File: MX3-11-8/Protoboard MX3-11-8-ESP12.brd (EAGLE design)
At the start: 74 x 99.4 mm, 638 parts, among them J1 DCJ0202, X3 RJ45

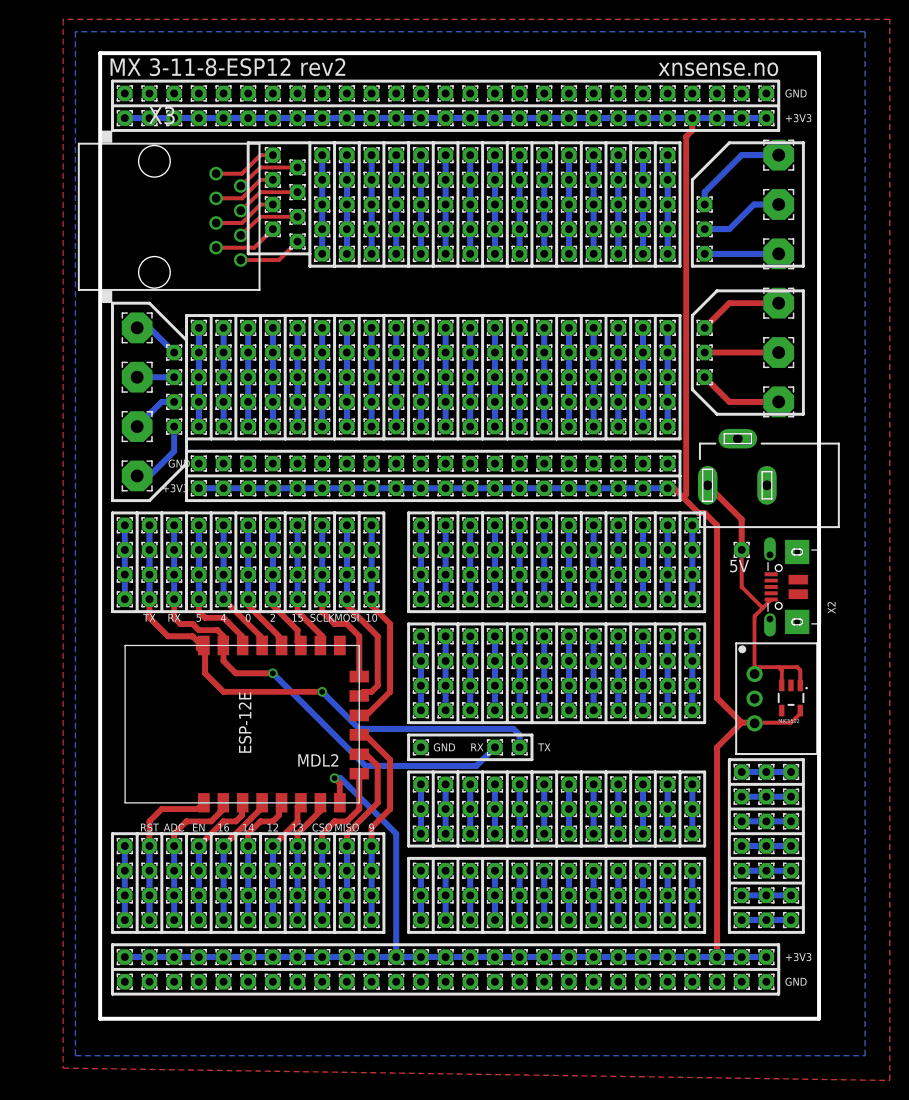
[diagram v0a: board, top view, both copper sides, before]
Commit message: Adjusted Polygon
Adjusted Polygon on all boxes. Changed length on MX-4-7-6 to fit the
box, it was 2mm to long.
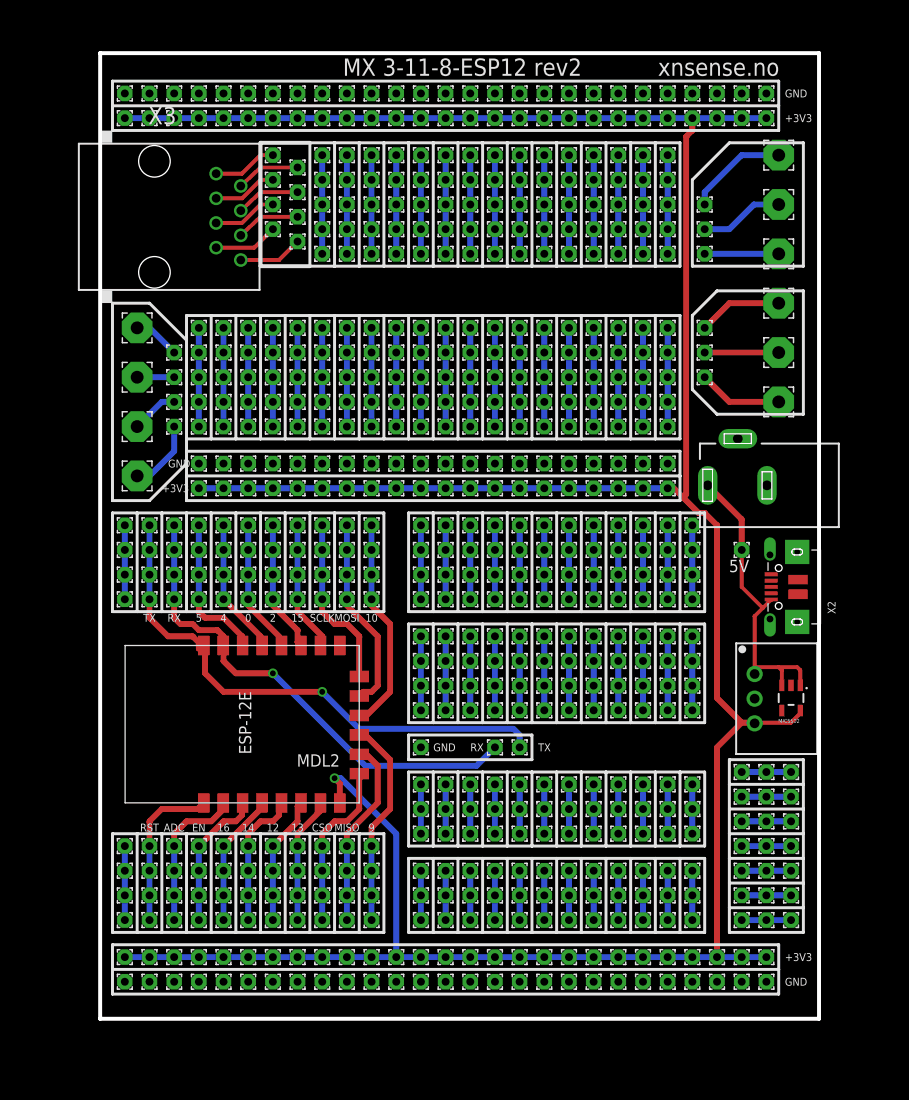
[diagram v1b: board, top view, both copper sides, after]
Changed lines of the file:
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@@
 <setting verticaltext="up"/>
 </settings>
-<grid distance="50" unitdist="mil" unit="mil" style="dots" multiple="1" display="yes" altdistance="5" altunitdist="mil" altunit="mil"/>
+<grid distance="50" unitdist="mil" unit="mil" style="dots" multiple="1" display="yes" altdistance="25" altunitdist="mil" altunit="mil"/>
 <layers>
 <layer number="1" name="Top" color="4" fill="1" visible="yes" active="yes"/>
@@
 <wire x1="74" y1="99.4" x2="74" y2="0" width="0.4064" layer="20"/>
 <text x="69.915" y="98.845" size="1.778" layer="25" rot="R180">xnsense.no</text>
-<text x="25.455" y="98.845" size="1.778" layer="25" rot="R180">MX 3-11-8-ESP12 rev2</text>
+<text x="49.585" y="98.845" size="1.778" layer="25" rot="R180">MX 3-11-8-ESP12 rev2</text>
 <wire x1="1.27" y1="96.52" x2="1.27" y2="93.98" width="0.3048" layer="25"/>
 <wire x1="1.27" y1="93.98" x2="69.85" y2="93.98" width="0.3048" layer="25"/>
@@
 <wire x1="1.27" y1="91.44" x2="69.85" y2="91.44" width="0.3048" layer="25"/>
 <wire x1="69.85" y1="91.44" x2="69.85" y2="93.98" width="0.3048" layer="25"/>
-<wire x1="15.24" y1="90.17" x2="21.59" y2="90.17" width="0.3048" layer="25"/>
-<wire x1="21.59" y1="90.17" x2="21.59" y2="78.74" width="0.3048" layer="25"/>
-<wire x1="21.59" y1="78.74" x2="15.24" y2="78.74" width="0.3048" layer="25"/>
-<wire x1="15.24" y1="78.74" x2="15.24" y2="90.17" width="0.3048" layer="25"/>
+<wire x1="21.59" y1="90.17" x2="21.59" y2="77.47" width="0.3048" layer="25"/>
 <wire x1="21.59" y1="90.17" x2="24.13" y2="90.17" width="0.3048" layer="25"/>
 <wire x1="24.13" y1="90.17" x2="24.13" y2="77.47" width="0.3048" layer="25"/>
 <wire x1="24.13" y1="77.47" x2="21.59" y2="77.47" width="0.3048" layer="25"/>
-<wire x1="21.59" y1="77.47" x2="21.59" y2="78.74" width="0.3048" layer="25"/>
 <wire x1="24.13" y1="77.47" x2="26.67" y2="77.47" width="0.3048" layer="25"/>
 <wire x1="26.67" y1="77.47" x2="29.21" y2="77.47" width="0.3048" layer="25"/>
@@
 <text x="6.35" y="54.61" size="0.8128" layer="25" align="center-left">+3V3</text>
 <text x="6.985" y="57.15" size="0.8128" layer="25" align="center-left">GND</text>
+<wire x1="21.59" y1="90.17" x2="16.51" y2="90.17" width="0.4064" layer="25"/>
+<wire x1="21.59" y1="77.47" x2="16.51" y2="77.47" width="0.4064" layer="25"/>
+<wire x1="16.51" y1="90.17" x2="16.51" y2="77.47" width="0.4064" layer="25"/>
+<dimension x1="0" y1="0" x2="0" y2="99.4" x3="-5.08" y3="49.7" textsize="1.778" layer="47"/>
+<dimension x1="0" y1="99.4" x2="74" y2="99.4" x3="37" y3="102.87" textsize="1.778" layer="47"/>
+<dimension x1="69.85" y1="96.52" x2="69.85" y2="99.4" x3="76.2" y3="97.96" textsize="1.778" layer="47"/>
+<dimension x1="69.85" y1="2.54" x2="69.85" y2="0" x3="77.47" y3="1.27" textsize="1.778" layer="47"/>
 </plain>
 <attributes>
@@
 <contactref element="DC" pad="2"/>
 <polygon width="0.4064" layer="1">
-<vertex x="-3.81" y="102.87"/>
-<vertex x="-3.81" y="-5.08"/>
-<vertex x="81.28" y="-6.35"/>
-<vertex x="81.28" y="102.87"/>
+<vertex x="0" y="99.4"/>
+<vertex x="0" y="0"/>
+<vertex x="74" y="0"/>
+<vertex x="74" y="99.4"/>
 </polygon>
 <contactref element="PAD27" pad="1"/>
@@
 <signal name="N$1">
 <polygon width="0.6096" layer="16">
-<vertex x="-2.54" y="101.6"/>
-<vertex x="-2.54" y="-3.81"/>
-<vertex x="78.74" y="-3.81"/>
-<vertex x="78.74" y="101.6"/>
+<vertex x="0" y="99.4"/>
+<vertex x="0" y="0"/>
+<vertex x="74" y="0"/>
+<vertex x="74" y="99.4"/>
 </polygon>
 </signal>

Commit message: Update to rev2
Updated to Pin headers instead of single wire pads
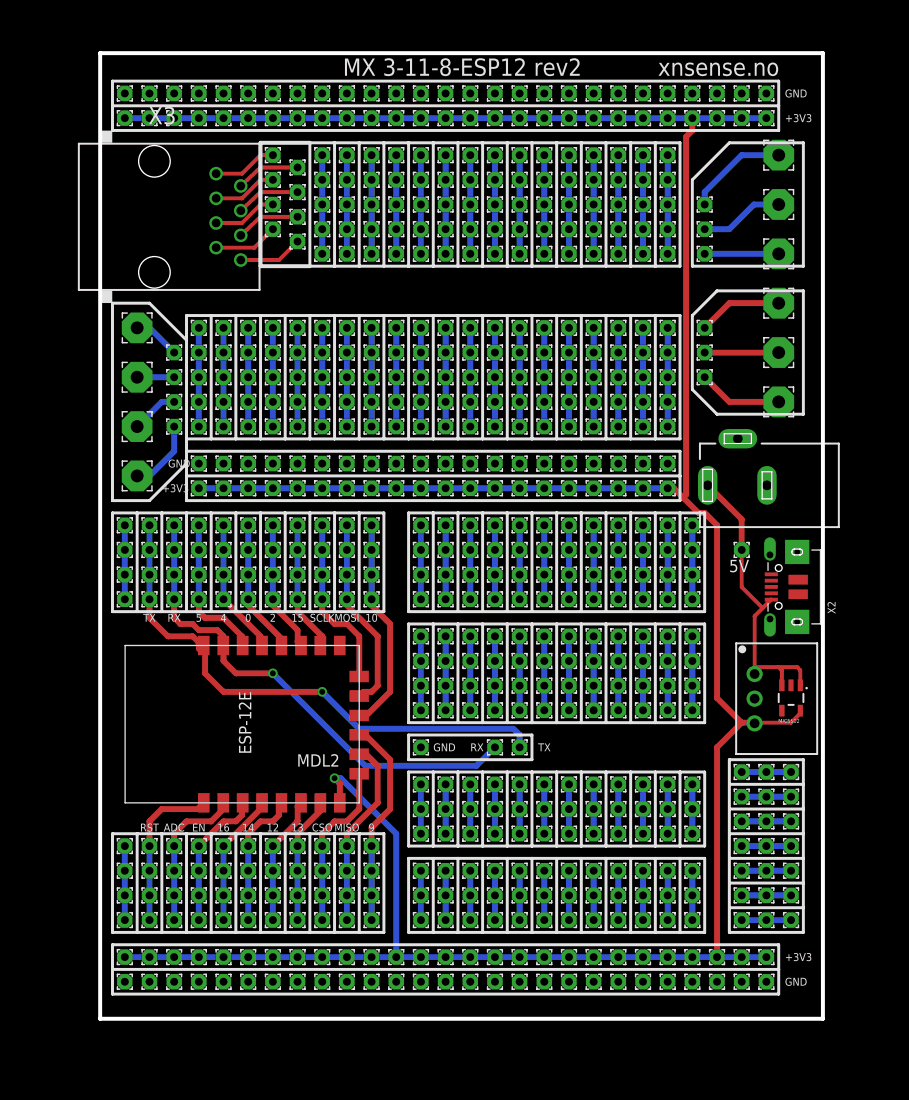
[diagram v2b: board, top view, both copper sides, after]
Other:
- board size 74 x 99.4 mm -> 74.4 x 99.4 mm
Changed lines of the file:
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@@
 <setting verticaltext="up"/>
 </settings>
-<grid distance="50" unitdist="mil" unit="mil" style="dots" multiple="1" display="yes" altdistance="25" altunitdist="mil" altunit="mil"/>
+<grid distance="50" unitdist="mil" unit="mm" style="dots" multiple="1" display="yes" altdistance="25" altunitdist="mil" altunit="mm"/>
 <layers>
 <layer number="1" name="Top" color="4" fill="1" visible="yes" active="yes"/>
@@
 <plain>
 <wire x1="0" y1="0" x2="0" y2="99.4" width="0.4064" layer="20"/>
-<wire x1="0" y1="0" x2="74" y2="0" width="0.4064" layer="20"/>
-<wire x1="74" y1="99.4" x2="0" y2="99.4" width="0.4064" layer="20"/>
-<wire x1="74" y1="99.4" x2="74" y2="0" width="0.4064" layer="20"/>
+<wire x1="0" y1="0" x2="74.4" y2="0" width="0.4064" layer="20"/>
+<wire x1="74.4" y1="99.4" x2="0" y2="99.4" width="0.4064" layer="20"/>
+<wire x1="74.4" y1="99.4" x2="74.4" y2="0" width="0.4064" layer="20"/>
 <text x="69.915" y="98.845" size="1.778" layer="25" rot="R180">xnsense.no</text>
 <text x="49.585" y="98.845" size="1.778" layer="25" rot="R180">MX 3-11-8-ESP12 rev2</text>
@@
 <wire x1="16.51" y1="90.17" x2="16.51" y2="77.47" width="0.4064" layer="25"/>
 <dimension x1="0" y1="0" x2="0" y2="99.4" x3="-5.08" y3="49.7" textsize="1.778" layer="47"/>
-<dimension x1="0" y1="99.4" x2="74" y2="99.4" x3="37" y3="102.87" textsize="1.778" layer="47"/>
+<dimension x1="0" y1="99.4" x2="74.4" y2="99.4" x3="37.2" y3="102.87" textsize="1.778" layer="47"/>
 <dimension x1="69.85" y1="96.52" x2="69.85" y2="99.4" x3="76.2" y3="97.96" textsize="1.778" layer="47"/>
 <dimension x1="69.85" y1="2.54" x2="69.85" y2="0" x3="77.47" y3="1.27" textsize="1.778" layer="47"/>
@@
 <vertex x="0" y="99.4"/>
 <vertex x="0" y="0"/>
-<vertex x="74" y="0"/>
-<vertex x="74" y="99.4"/>
+<vertex x="74.4" y="0"/>
+<vertex x="74.4" y="99.4"/>
 </polygon>
 <contactref element="PAD27" pad="1"/>
@@
 <vertex x="0" y="99.4"/>
 <vertex x="0" y="0"/>
-<vertex x="74" y="0"/>
-<vertex x="74" y="99.4"/>
+<vertex x="74.4" y="0"/>
+<vertex x="74.4" y="99.4"/>
 </polygon>
 </signal>
